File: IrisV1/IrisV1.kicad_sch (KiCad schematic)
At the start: 59 parts, among them J1 Conn_02x02_Odd_Even, J13 TB002-500-02BE, J3 USB4110GFA, J4 Conn_01x04, J5 MSD-10-C, J6 MSD-10-C, J7 Conn_02x02_Odd_Even, U2 ESDS302DBVR, U22 TPS63070RNMR, U3 ESP32-S3-WROOM-1U-N4

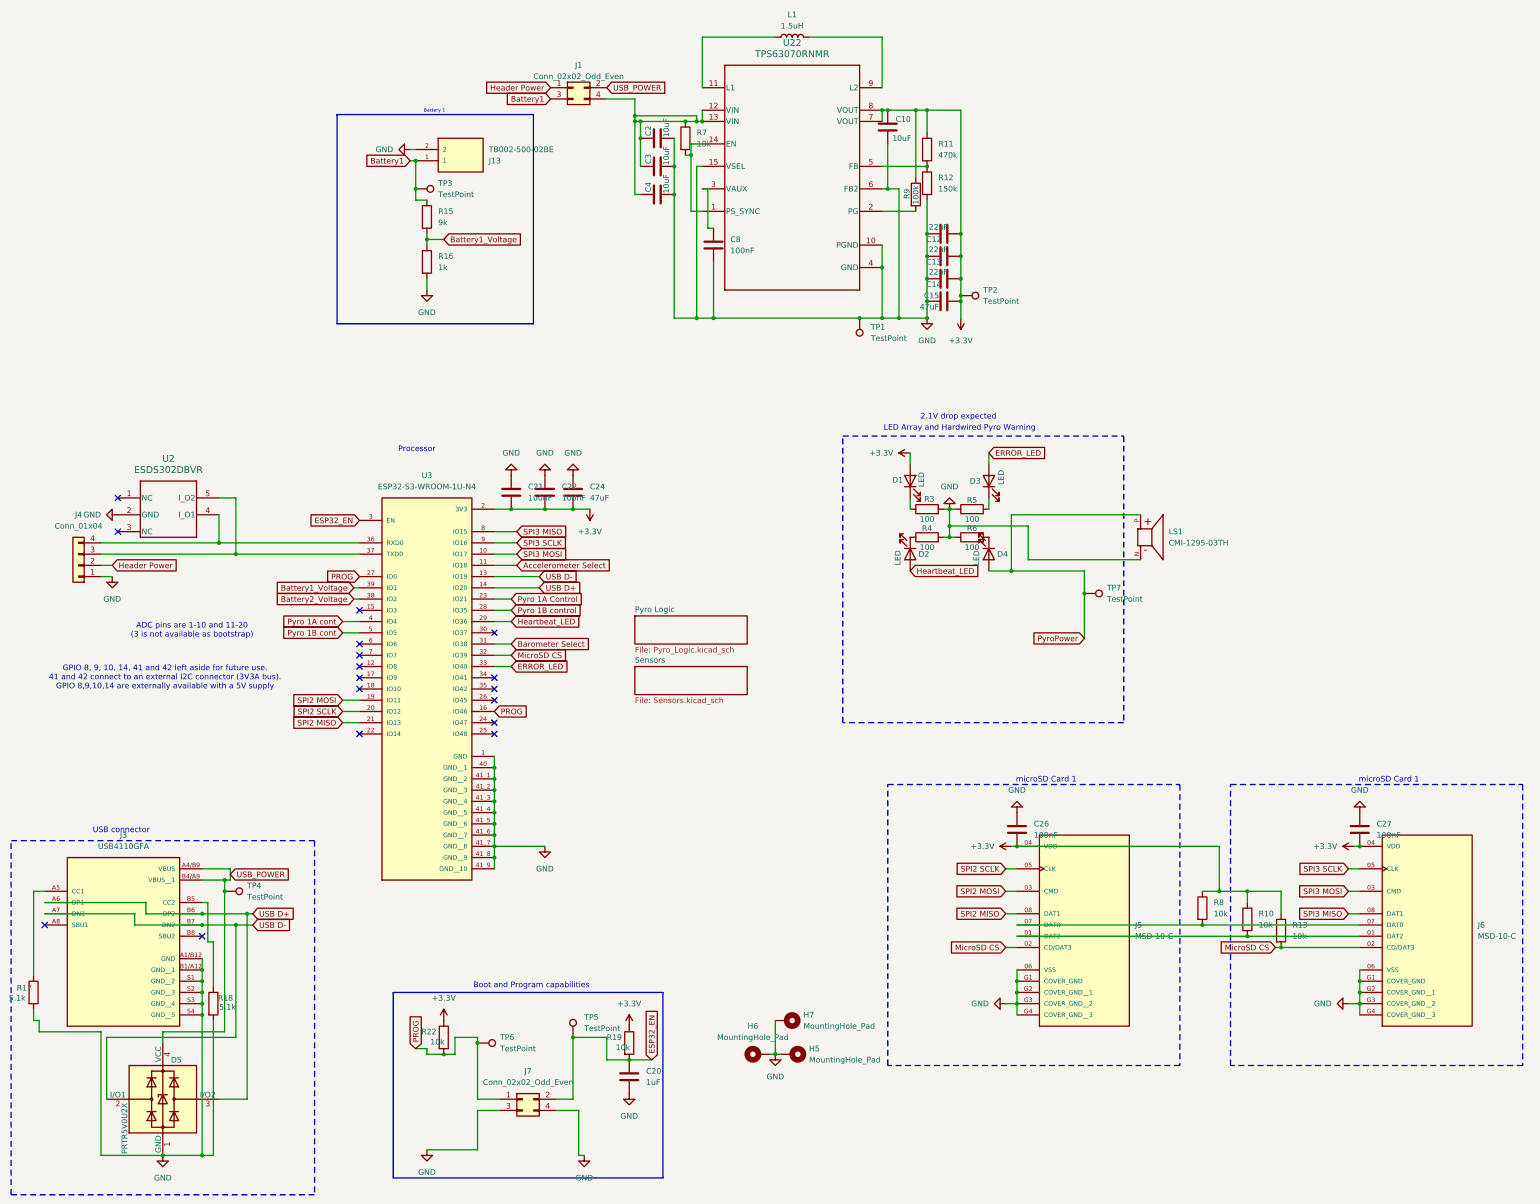
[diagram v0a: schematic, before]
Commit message: Symbol changes to use common library in Iris
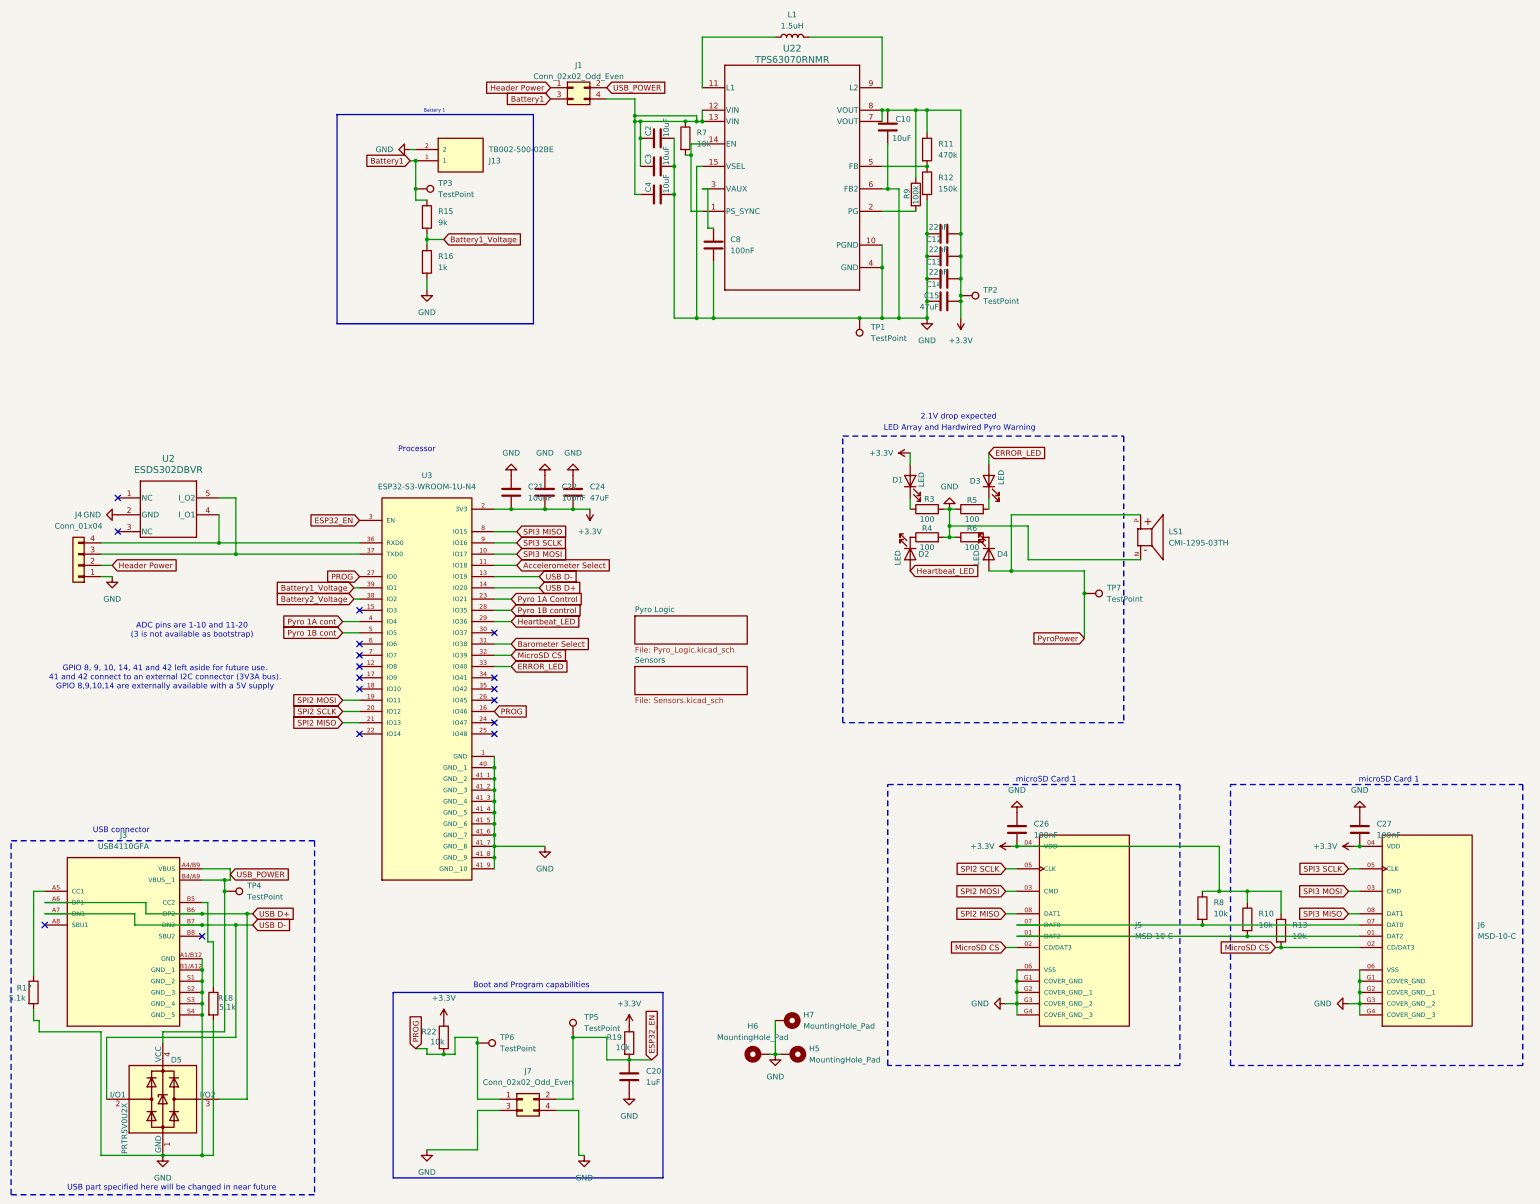
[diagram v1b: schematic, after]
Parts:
- J13: footprint screw terminal:CUI_TB002-500-02BE -> UNSW Rocketry Library:CUI_TB002-500-02BE; symbol screw terminal:TB002-500-02BE -> UNSW Rocketry library:TB002-500-02BE
- J3: footprint USB:GCT_USB4110GFA -> UNSW Rocketry Library:GCT_USB4110GFA; symbol USB Connector:USB4110GFA -> UNSW Rocketry library:USB4110GFA
- J5, J6: footprint microSd card locking:CUI_MSD-10-C -> UNSW Rocketry Library:CUI_MSD-10-C; symbol MicroSD card hinged:MSD-10-C -> UNSW Rocketry library:MSD-10-C
- L1: footprint inductor:1277AS-H-1R0M=P2_MUR-M -> UNSW Rocketry Library:1277AS-H-1R0M=P2_MUR-M
- LS1: footprint low volt buzzer:SPKR_CMI-1295-03TH -> UNSW Rocketry Library:SPKR_CMI-1295-03TH; symbol low volt buzzer:CMI-1295-03TH -> UNSW Rocketry library:CMI-1295-03TH
- U2: footprint esd:DBV0005A_L -> UNSW Rocketry Library:DBV0005A_N; symbol 3V3 ESD:ESDS302DBVR -> UNSW Rocketry library:ESDS302DBVR
- U22: footprint TPS63070:RNM0015A -> UNSW Rocketry Library:RNM0015A; symbol TPS63070:TPS63070RNMR -> UNSW Rocketry library:TPS63070RNMR
- U3: footprint ESP32-S3:XCVR_ESP32-S3-WROOM-1U-N4 -> UNSW Rocketry Library:XCVR_ESP32-S3-WROOM-1U-N4; symbol ESP32-S3:ESP32-S3-WROOM-1U-N4 -> UNSW Rocketry library:ESP32-S3-WROOM-1U-N4
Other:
- note added: "USB part specified here will be changed in near future"
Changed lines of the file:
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@@
 		)
 	)
+	(text "USB part specified here will be changed in near future"
+		(exclude_from_sim no)
+		(at 55.372 192.786 0)
+		(effects
+			(font
+				(size 1.27 1.27)
+			)
+		)
+	)
 	(text "Processor"
 		(exclude_from_sim no)
@@
 	)
 	(symbol
-		(lib_id "ESP32-S3:ESP32-S3-WROOM-1U-N4")
+		(lib_id "UNSW Rocketry library:ESP32-S3-WROOM-1U-N4")
 		(at 113.03 67.31 0)
 		(unit 1)
@@
 			)
 		)
-		(property "Footprint" "ESP32-S3:XCVR_ESP32-S3-WROOM-1U-N4"
+		(property "Footprint" "UNSW Rocketry Library:XCVR_ESP32-S3-WROOM-1U-N4"
 			(at 113.03 67.31 0)
 			(hide yes)
@@
 	)
 	(symbol
-		(lib_id "USB Connector:USB4110GFA")
+		(lib_id "UNSW Rocketry library:USB4110GFA")
 		(at 44.45 128.27 0)
 		(unit 1)
@@
 			)
 		)
-		(property "Footprint" "USB:GCT_USB4110GFA"
+		(property "Footprint" "UNSW Rocketry Library:GCT_USB4110GFA"
 			(at 44.45 128.27 0)
 			(hide yes)
@@
 	)
 	(symbol
-		(lib_id "screw terminal:TB002-500-02BE")
+		(lib_id "UNSW Rocketry library:TB002-500-02BE")
 		(at 120.65 -41.91 0)
 		(mirror x)
@@
 			)
 		)
-		(property "Footprint" "screw terminal:CUI_TB002-500-02BE"
+		(property "Footprint" "UNSW Rocketry Library:CUI_TB002-500-02BE"
 			(at 120.65 -41.91 0)
 			(hide yes)
@@
 	)
 	(symbol
-		(lib_id "3V3 ESD:ESDS302DBVR")
+		(lib_id "UNSW Rocketry library:ESDS302DBVR")
 		(at 54.61 43.18 0)
 		(unit 1)
@@
 			)
 		)
-		(property "Footprint" "esd:DBV0005A_L"
+		(property "Footprint" "UNSW Rocketry Library:DBV0005A_N"
 			(at 54.61 43.18 0)
 			(hide yes)
@@
 	)
 	(symbol
-		(lib_id "MicroSD card hinged:MSD-10-C")
+		(lib_id "UNSW Rocketry library:MSD-10-C")
 		(at 339.09 130.81 0)
 		(unit 1)
@@
 			)
 		)
-		(property "Footprint" "microSd card locking:CUI_MSD-10-C"
+		(property "Footprint" "UNSW Rocketry Library:CUI_MSD-10-C"
 			(at 339.09 130.81 0)
 			(hide yes)
@@
 	)
 	(symbol
-		(lib_id "low volt buzzer:CMI-1295-03TH")
+		(lib_id "UNSW Rocketry library:CMI-1295-03TH")
 		(at 276.86 45.72 0)
 		(unit 1)
@@
 			)
 		)
-		(property "Footprint" "low volt buzzer:SPKR_CMI-1295-03TH"
+		(property "Footprint" "UNSW Rocketry Library:SPKR_CMI-1295-03TH"
 			(at 276.86 45.72 0)
 			(hide yes)
@@
 	)
 	(symbol
-		(lib_id "MicroSD card hinged:MSD-10-C")
+		(lib_id "UNSW Rocketry library:MSD-10-C")
 		(at 261.62 130.81 0)
 		(unit 1)
@@
 			)
 		)
-		(property "Footprint" "microSd card locking:CUI_MSD-10-C"
+		(property "Footprint" "UNSW Rocketry Library:CUI_MSD-10-C"
 			(at 261.62 130.81 0)
 			(hide yes)
@@
 	)
 	(symbol
-		(lib_id "TPS63070:TPS63070RNMR")
+		(lib_id "UNSW Rocketry library:TPS63070RNMR")
 		(at 195.58 -35.56 0)
 		(unit 1)
@@
 		(fields_autoplaced yes)
 		(property "Reference" "U22"
-			(at 195.58 -66.04 0)
+			(at 195.58 -64.77 0)
 			(show_name no)
 			(do_not_autoplace no)
@@
 		)
 		(property "Value" "TPS63070RNMR"
-			(at 195.58 -63.5 0)
+			(at 195.58 -62.23 0)
 			(show_name no)
 			(do_not_autoplace no)
@@
 			)
 		)
-		(property "Footprint" "TPS63070:RNM0015A"
+		(property "Footprint" "UNSW Rocketry Library:RNM0015A"
 			(at 195.58 -35.56 0)
 			(hide yes)
@@
 			)
 		)
-		(property "Footprint" "inductor:1277AS-H-1R0M=P2_MUR-M"
+		(property "Footprint" "UNSW Rocketry Library:1277AS-H-1R0M=P2_MUR-M"
 			(at 195.58 -67.31 0)
 			(hide yes)

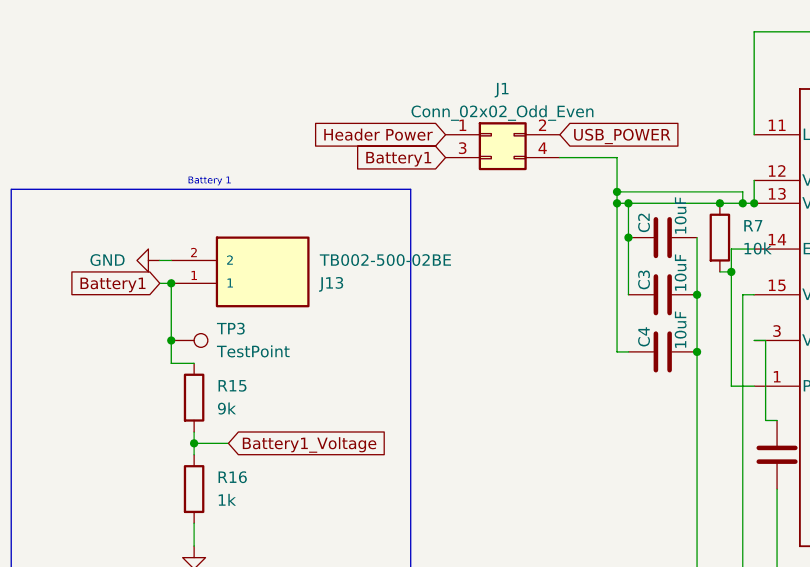
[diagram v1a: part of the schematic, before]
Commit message: Changed to 3.5mm Screw terminals
All screw terminals in IRIS changed to 3.5mm screw terminals per Oliver's request.
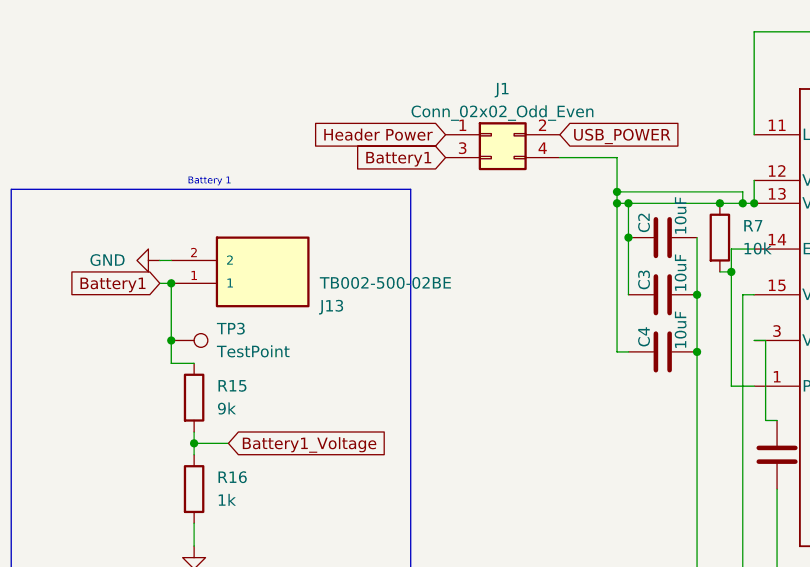
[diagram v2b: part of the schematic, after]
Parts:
- J13: footprint UNSW Rocketry Library:CUI_TB002-500-02BE -> UNSW Rocketry Library:ADAMTECH_EBWA-02-A; symbol UNSW Rocketry library:TB002-500-02BE -> UNSW Rocketry library:EBWA-02-A; MANUFACTURER CUI -> AdamTech; MAXIMUM_PACKAGE_HEIGHT (none) -> 8.5mm; PARTREV (none) -> A
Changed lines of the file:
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@@
 	)
 	(junction
+		(at 110.49 -39.37)
+		(diameter 0)
+		(color 0 0 0 0)
+	)
+	(junction
 		(at 158.75 163.83)
 		(diameter 0)
@@
 	)
 	(junction
-		(at 110.49 -39.37)
-		(diameter 0)
-		(color 0 0 0 0)
-	)
-	(junction
 		(at 168.91 -31.75)
 		(diameter 0)
@@
 	(wire
 		(pts
-			(xy 109.22 -41.91) (xy 110.49 -41.91)
-		)
-		(stroke
-			(width 0)
-			(type default)
-		)
-	)
-	(wire
-		(pts
 			(xy 110.49 -33.02) (xy 110.49 -39.37)
 		)
@@
 	(wire
 		(pts
+			(xy 109.22 -41.91) (xy 110.49 -41.91)
+		)
+		(stroke
+			(width 0)
+			(type default)
+		)
+	)
+	(wire
+		(pts
 			(xy 153.67 163.83) (xy 158.75 163.83)
 		)
@@
 	)
 	(symbol
-		(lib_id "UNSW Rocketry library:TB002-500-02BE")
-		(at 120.65 -41.91 0)
+		(lib_id "UNSW Rocketry library:EBWA-02-A")
+		(at 120.65 -39.37 0)
 		(mirror x)
 		(unit 1)
@@
 		(dnp no)
 		(property "Reference" "J13"
-			(at 127 -39.3699 0)
+			(at 127 -36.8299 0)
 			(show_name no)
 			(do_not_autoplace no)
@@
 		)
 		(property "Value" "TB002-500-02BE"
-			(at 127 -41.9099 0)
+			(at 127 -39.3699 0)
 			(show_name no)
 			(do_not_autoplace no)
@@
 			)
 		)
-		(property "Footprint" "UNSW Rocketry Library:CUI_TB002-500-02BE"
-			(at 120.65 -41.91 0)
+		(property "Footprint" "UNSW Rocketry Library:ADAMTECH_EBWA-02-A"
+			(at 120.65 -39.37 0)
 			(hide yes)
 			(show_name no)
@@
 		)
 		(property "Datasheet" ""
-			(at 120.65 -41.91 0)
+			(at 120.65 -39.37 0)
 			(hide yes)
 			(show_name no)
@@
 		)
 		(property "Description" ""
-			(at 120.65 -41.91 0)
+			(at 120.65 -39.37 0)
 			(hide yes)
 			(show_name no)
@@
 		)
 		(property "STANDARD" "Manufacturer Recommendations"
-			(at 120.65 -41.91 0)
+			(at 120.65 -39.37 0)
 			(hide yes)
 			(show_name no)
@@
 			)
 		)
-		(property "MANUFACTURER" "CUI"
-			(at 120.65 -41.91 0)
+		(property "MANUFACTURER" "AdamTech"
+			(at 120.65 -39.37 0)
 			(hide yes)
 			(show_name no)
@@
 		)
 		(property "Check_prices" ""
-			(at 120.65 -41.91 0)
+			(at 120.65 -39.37 0)
 			(hide yes)
 			(show_name no)
@@
 		)
 		(property "Description_1" ""
-			(at 120.65 -41.91 0)
+			(at 120.65 -39.37 0)
 			(hide yes)
 			(show_name no)
@@
 		)
 		(property "Purchase-URL" ""
-			(at 120.65 -41.91 0)
+			(at 120.65 -39.37 0)
 			(hide yes)
 			(show_name no)
@@
 		)
 		(property "SnapEDA_Link" ""
-			(at 120.65 -41.91 0)
+			(at 120.65 -39.37 0)
 			(hide yes)
 			(show_name no)
@@
 			)
 		)
+		(property "PARTREV" "A"
+			(at 120.65 -39.37 0)
+			(hide yes)
+			(show_name no)
+			(do_not_autoplace no)
+			(effects
+				(font
+					(size 1.27 1.27)
+				)
+				(justify bottom)
+			)
+		)
+		(property "MAXIMUM_PACKAGE_HEIGHT" "8.5mm"
+			(at 120.65 -39.37 0)
+			(hide yes)
+			(show_name no)
+			(do_not_autoplace no)
+			(effects
+				(font
+					(size 1.27 1.27)
+				)
+				(justify bottom)
+			)
+		)
